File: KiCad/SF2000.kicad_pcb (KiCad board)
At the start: 4 copper layers, 111.5 x 83.9 mm, 73 parts, among them J1 Conn_2Rows-86Pins_even_odd, J2 Conn_01x02, J3 Conn_02x03_Odd_Even, J4 Conn_02x01, J5 IDE_ATA_44pin, J6 Micro_SD_Card_Socket, J8 Conn_02x01, J9 Conn_02x01, U1 LM1117-3.3, U10 IS61WV20488FBLL-10TLI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

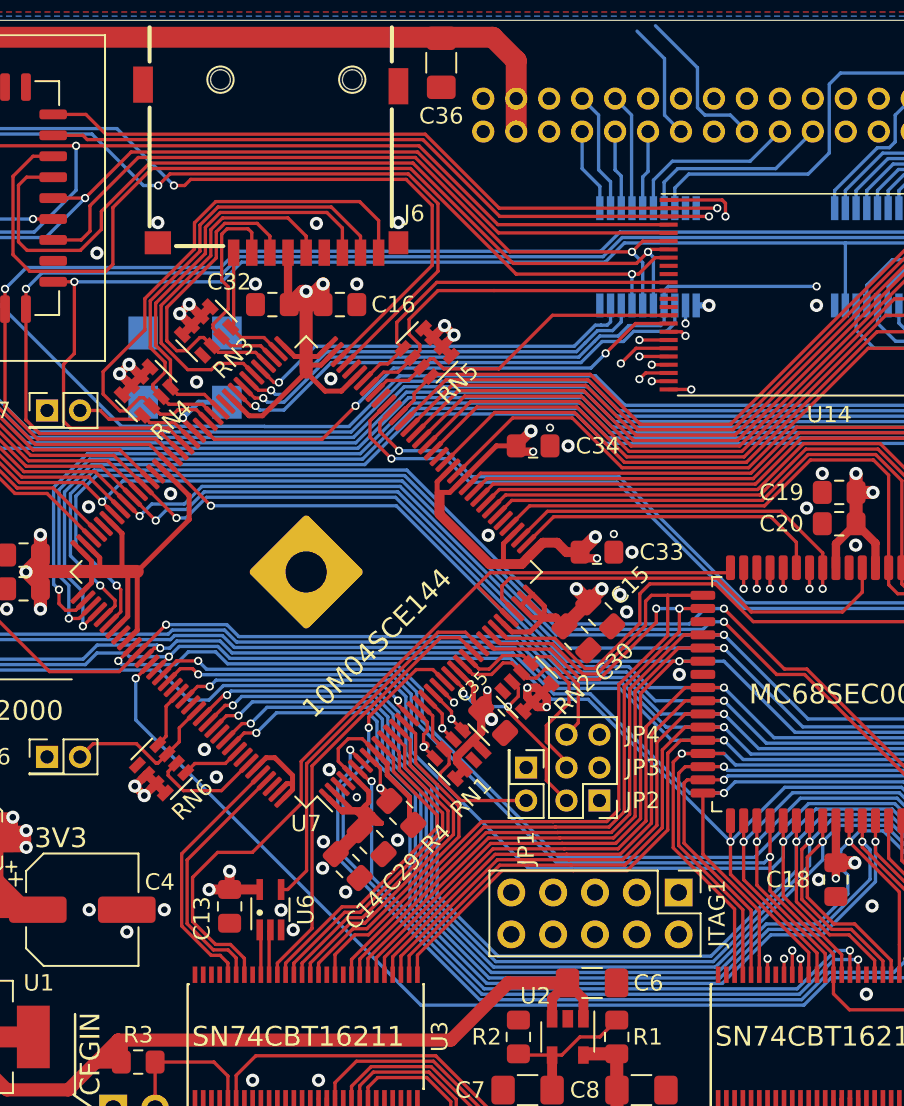
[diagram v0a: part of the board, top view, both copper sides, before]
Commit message: more routing and added two capacitors
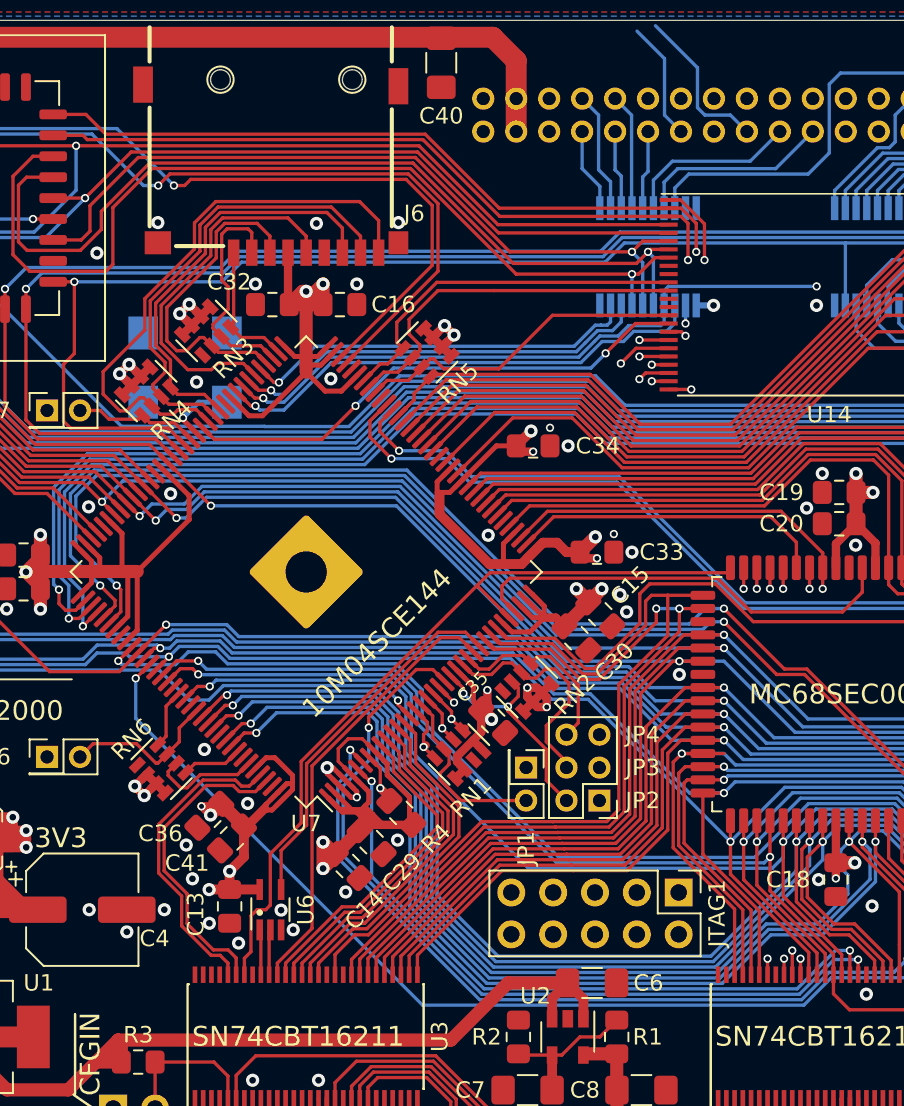
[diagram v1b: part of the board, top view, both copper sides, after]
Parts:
- added C36: 0.01uF, Capacitor_SMD:C_0805_2012Metric_Pad1.15x1.40mm_HandSolder, F.Cu at (122.1, 107.4)
- added C41: 0.1uF, Capacitor_SMD:C_0805_2012Metric_Pad1.15x1.40mm_HandSolder, F.Cu at (123.5, 108.8)
- renumbered C36 to C40
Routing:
- net 3V3: track 292.6 -> 313.6 mm, vias 47 -> 49
- net GND: track 91.2 -> 96.7 mm, vias 79 -> 83
- net FC2_3V3: track 52.9 -> 48.8 mm
- net CFGIN_3V3: track 15.5 -> 19.0 mm
- net CFGOUT_3V3: track 15.6 -> 18.9 mm
- net A16_3V3: track 183.2 -> 180.7 mm
- net A15_3V3: track 180.7 -> 178.4 mm
- net A14_3V3: track 179.9 -> 177.9 mm

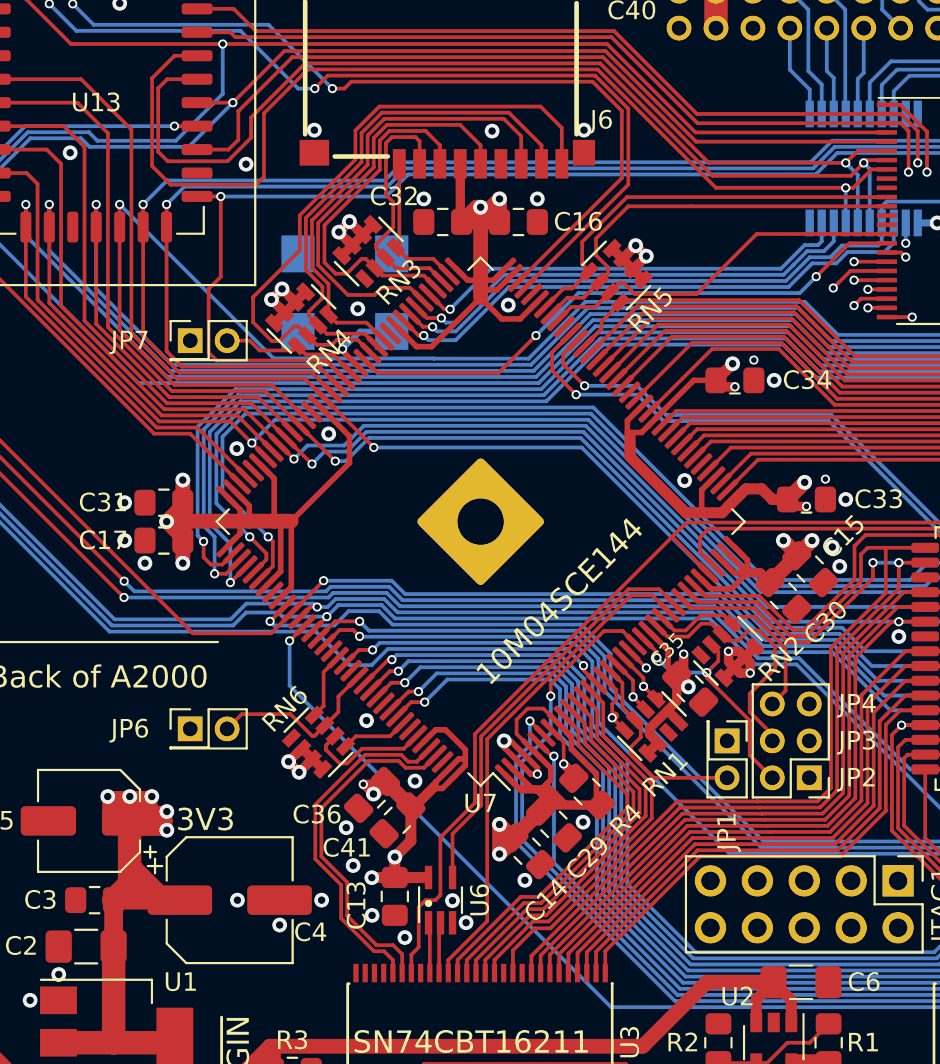
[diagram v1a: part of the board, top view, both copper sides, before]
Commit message: Fixed Switch and Jumper enumeration and silkscreen
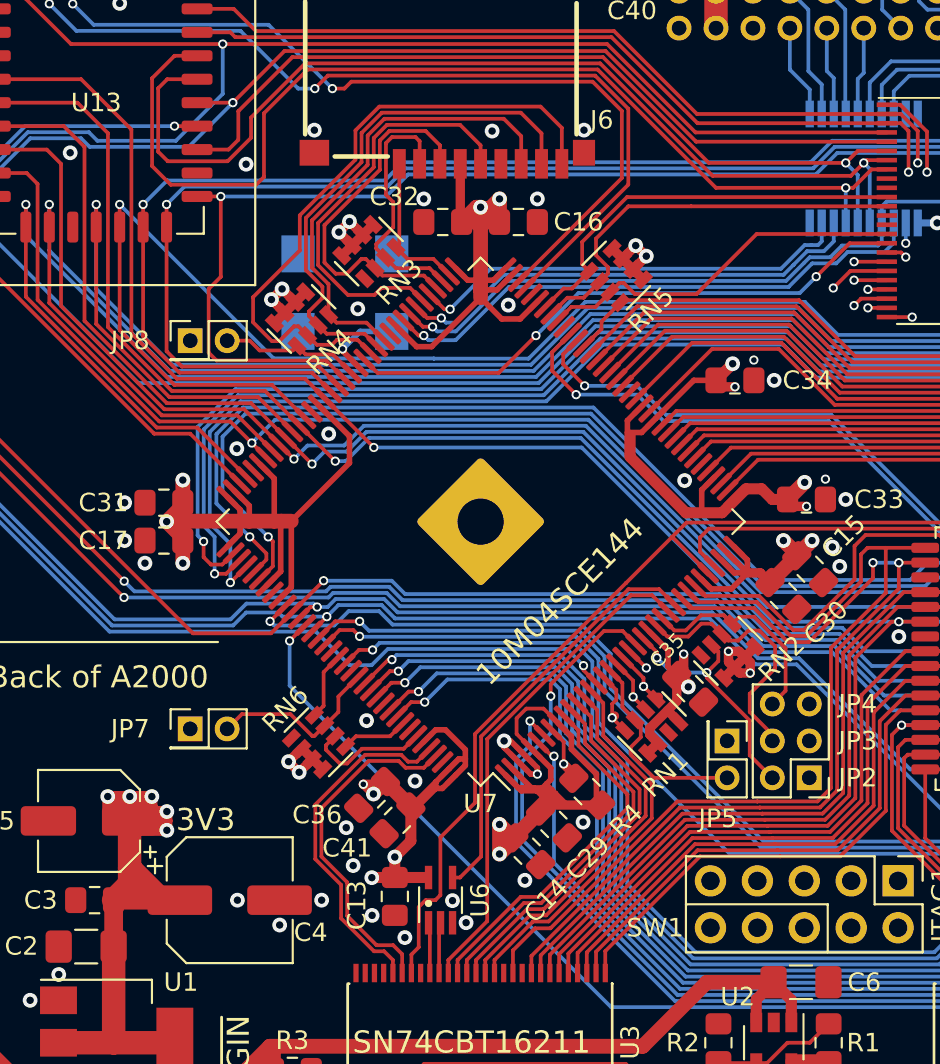
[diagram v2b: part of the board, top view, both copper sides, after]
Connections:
- J4 pad 2: JP1 -> JP5
- J8 pad 2: JP6 -> JP7
- J9 pad 2: JP7 -> JP8
- JTAG1 pad 8: JP5 -> SW1
- R4 pad 2: JP5 -> SW1
- RN1 pad 3: JP1 -> JP5
- RN4 pad 1: JP7 -> JP8
- RN6 pad 3: JP6 -> JP7
- U7 pad 129: JP6 -> JP7
- U7 pad 17: JP1 -> JP5
- U7 pad 8: JP5 -> SW1
- U7 pad 89: JP7 -> JP8
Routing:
- net SW1: track 0.00 -> 18.6 mm, vias 0 -> 1
- net JP1: track 11.2 -> 0.00 mm
- net JP6: track 9.70 -> 0.00 mm
- net JP8: track 0.00 -> 7.63 mm
- net JP5: track 18.6 -> 11.2 mm, vias 1 -> 0
- net JP7: track 7.63 -> 9.70 mm
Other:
- board text added: "JP5"
- board text added: "JP8"
- board text added: "SW1"
- board text removed: "JP1"
- board text removed: "JP6"

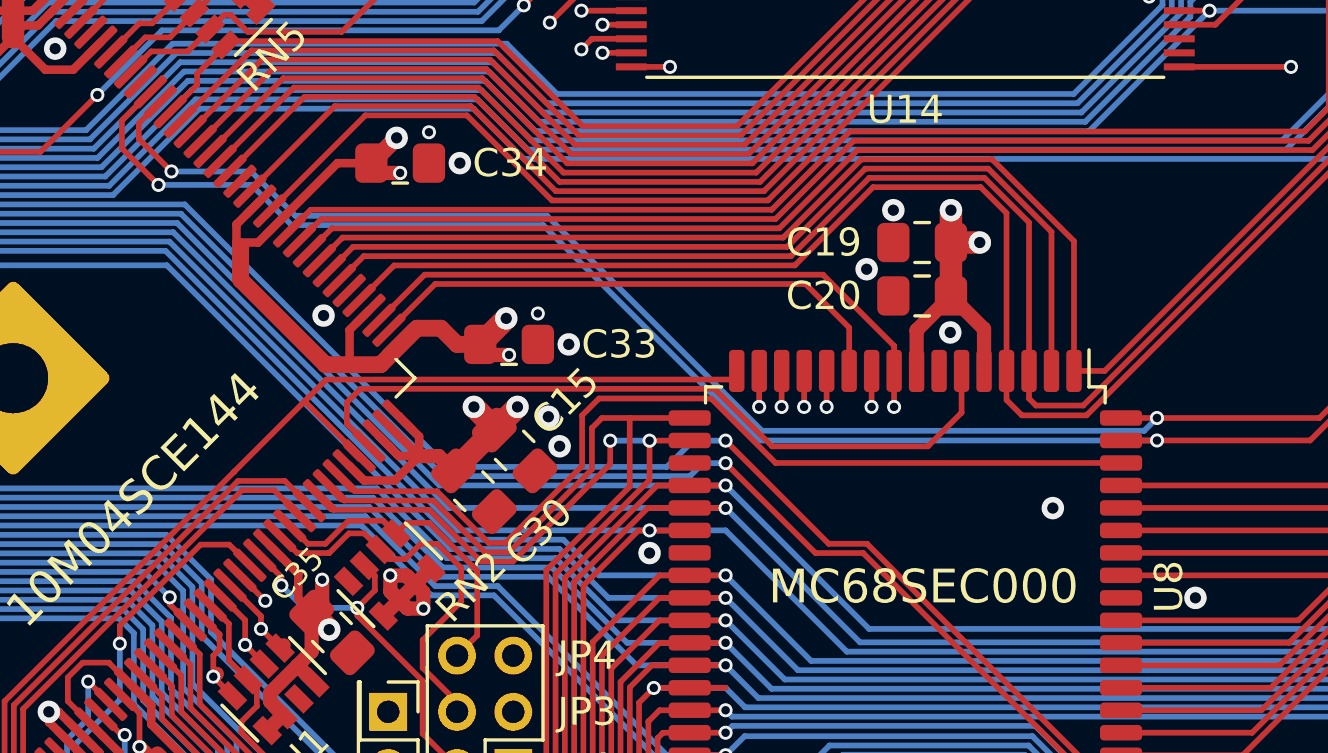
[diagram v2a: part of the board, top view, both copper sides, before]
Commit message: fixed JP6
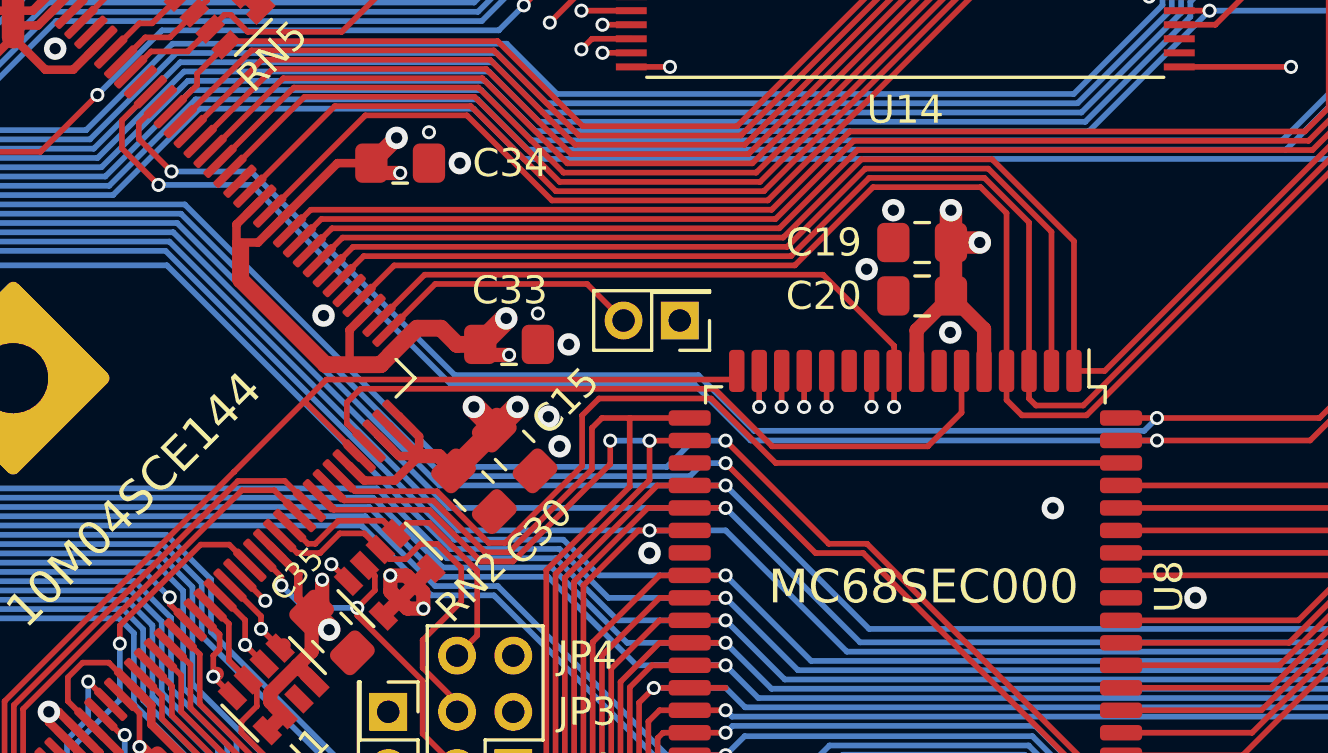
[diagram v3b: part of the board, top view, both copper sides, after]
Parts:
- added J8: Conn_02x01, Connector_PinHeader_2.00mm:PinHeader_2x01_P2.00mm_Vertical, F.Cu at (151.7, 90.5)
- renumbered J9 to J10, J8 to J9
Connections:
- RN2 pad 4: Net-(RN2-Pad4) -> JP6
- U7 pad 38: AVEC_3V3 -> JP6
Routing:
- net JP6: track 0.00 -> 25.4 mm, vias 0 -> 1
- net AVEC_3V3: track 19.2 -> 0.00 mm
- net A6_3V3: track 210.7 -> 215.3 mm
- net A4_3V3: track 191.7 -> 196.0 mm
- net A7_3V3: track 211.9 -> 216.3 mm
- net A5_3V3: track 193.9 -> 197.8 mm
- net A9_3V3: track 184.3 -> 186.2 mm
- net A8_3V3: track 217.8 -> 219.7 mm
- net A14_3V3: track 177.9 -> 178.7 mm
- net A15_3V3: track 178.4 -> 179.2 mm
- net A16_3V3: track 180.7 -> 181.5 mm
- net A11_3V3: track 182.6 -> 183.2 mm
- net A10_3V3: track 178.5 -> 179.1 mm
- net A3_3V3: track 184.6 -> 184.0 mm

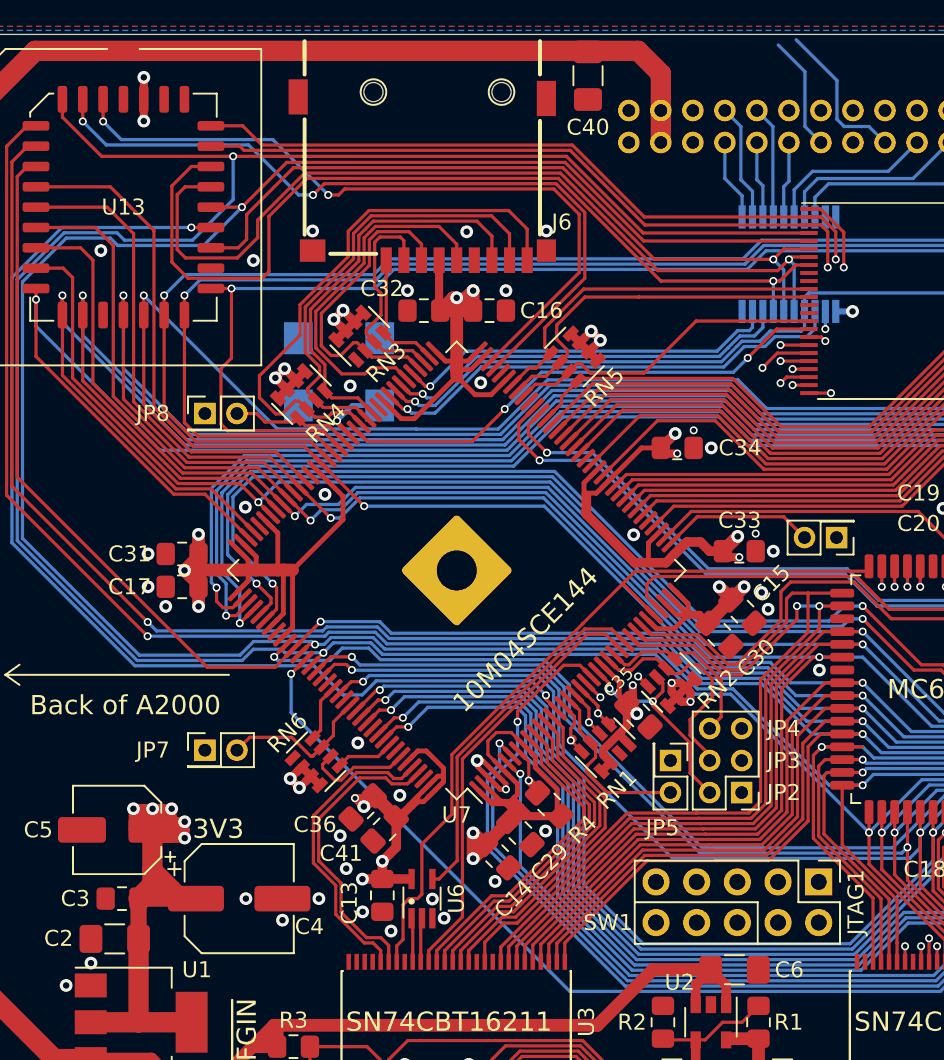
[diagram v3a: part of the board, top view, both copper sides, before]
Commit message: added ROM_WE signal/pin to FPGA, removed XRDY-signal/pin, and some silkscreen fixes
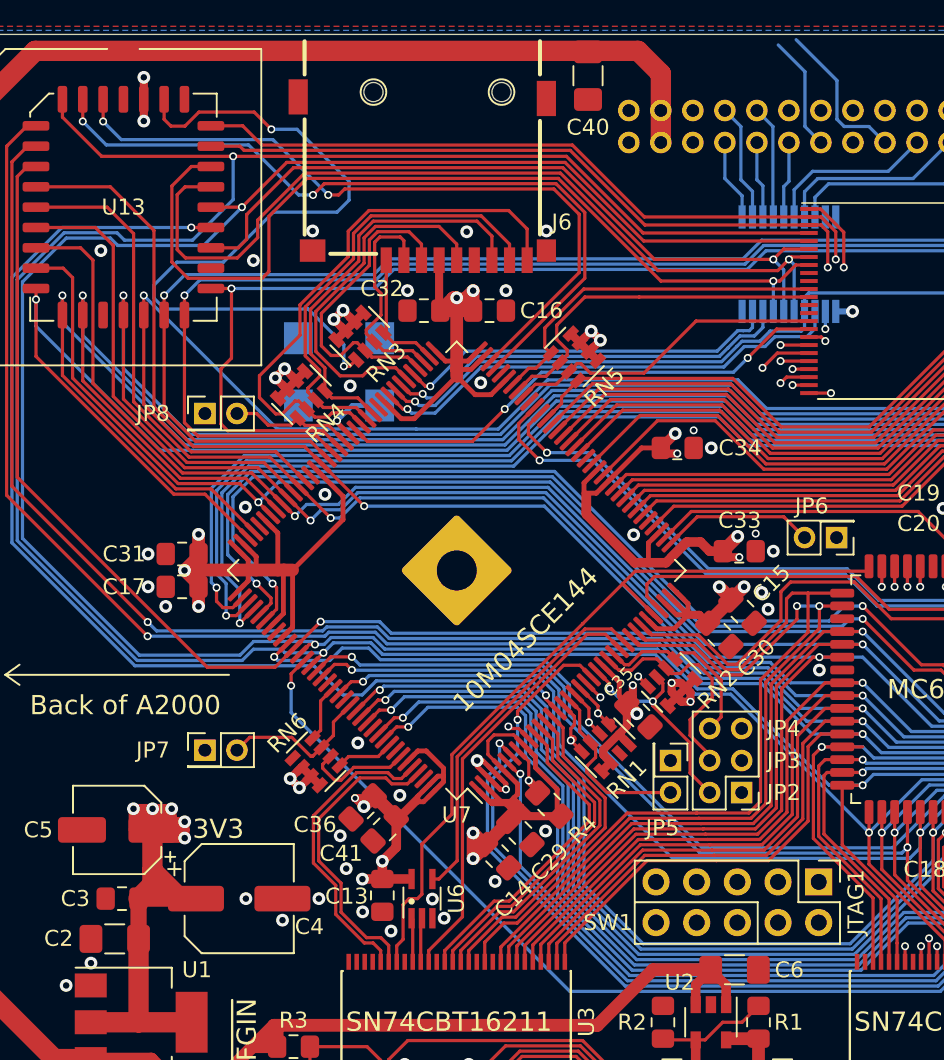
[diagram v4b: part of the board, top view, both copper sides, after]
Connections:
- RN3 pad 1: Net-(RN3-Pad1) -> ROM_WE
- U13 pad 31: 3V3 -> ROM_WE
- U7 pad 10: XRDY_3V3 -> ROM_WE
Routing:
- net ROM_WE: track 0.00 -> 75.8 mm, vias 0 -> 3
- net XRDY_3V3: track 19.7 -> 0.00 mm
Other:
- board text added: "JP6"
